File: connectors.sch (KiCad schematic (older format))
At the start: 40 parts, among them J10 70543-0001, J11 70543-0001, J12 70543-0001, J13 70543-0001, J14 70543-0003, J15 Conn_02x20_Odd_Even, J5 20021121-00010C4LF, J6 70543-0001, J7 70543-0001, J8 70543-0001, J9 70543-0001

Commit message: Current snapshot
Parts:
- renumbered C31 to C30, C32 to C31, C33 to C32, C34 to C33
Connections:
- net Z_OA1 renamed Z_BMB1
- net Z_OA2 renamed Z_BMB2
- net Z_OB1 renamed Z_BMA1
- net Z_OB2 renamed Z_BMA2
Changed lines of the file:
@@
 $Descr A4 11693 8268
 encoding utf-8
-Sheet 5 7
+Sheet 5 11
 Title "Connectors"
 Date ""
@@
 $EndComp
 $Comp
-L Device:C C31
+L Device:C C30
 U 1 1 5B1719D4
 P 1050 3450
-F 0 "C31" H 1165 3496 50  0000 L CNN
+F 0 "C30" H 1165 3496 50  0000 L CNN
 F 1 "100nF" H 1165 3405 50  0000 L CNN
 F 2 "Capacitor_SMD:C_0603_1608Metric" H 1088 3300 50  0001 C CNN
@@
 Text HLabel 4050 5700 0    50   Input ~ 0
 Y_MIN
-Text HLabel 4600 1300 0    50   Input ~ 0
-FAN1_OUT
 Text GLabel 4600 1400 0    50   Input ~ 0
 VDD_FAN
@@
 $EndComp
 Text HLabel 4600 3000 0    50   Input ~ 0
-Z_OA1
+Z_BMB1
 Text HLabel 4600 3100 0    50   Input ~ 0
-Z_OA2
+Z_BMB2
 Text HLabel 4600 3300 0    50   Input ~ 0
-Z_OB2
+Z_BMA2
 Text HLabel 4600 3200 0    50   Input ~ 0
-Z_OB1
-Text HLabel 4600 1600 0    50   Input ~ 0
-FAN2_OUT
+Z_BMA1
 Text GLabel 4600 1700 0    50   Input ~ 0
 VDD_FAN
@@
 	2150 4500 2150 4400
 $Comp
-L Device:C C32
+L Device:C C31
 U 1 1 5B56580A
 P 1050 4650
-F 0 "C32" H 1165 4696 50  0000 L CNN
+F 0 "C31" H 1165 4696 50  0000 L CNN
 F 1 "100nF" H 1165 4605 50  0000 L CNN
 F 2 "Capacitor_SMD:C_0603_1608Metric" H 1088 4500 50  0001 C CNN
@@
 	2150 5700 2150 5600
 $Comp
-L Device:C C33
+L Device:C C32
 U 1 1 5B57C5D0
 P 1050 5850
-F 0 "C33" H 1165 5896 50  0000 L CNN
+F 0 "C32" H 1165 5896 50  0000 L CNN
 F 1 "100nF" H 1165 5805 50  0000 L CNN
 F 2 "Capacitor_SMD:C_0603_1608Metric" H 1088 5700 50  0001 C CNN
@@
 	2150 6900 2150 6800
 $Comp
-L Device:C C34
+L Device:C C33
 U 1 1 5BC983BD
 P 1050 7050
-F 0 "C34" H 1165 7096 50  0000 L CNN
+F 0 "C33" H 1165 7096 50  0000 L CNN
 F 1 "100nF" H 1165 7005 50  0000 L CNN
 F 2 "Capacitor_SMD:C_0603_1608Metric" H 1088 6900 50  0001 C CNN
@@
 	1    0    0    -1
 $EndComp
-Text HLabel 4600 1900 0    50   Input ~ 0
-FAN3_OUT
 Text GLabel 4600 2000 0    50   Input ~ 0
 VDD_FAN
-Text HLabel 4600 2200 0    50   Input ~ 0
-FAN4_OUT
 Text GLabel 4600 2300 0    50   Input ~ 0
 VDD_FAN
@@
 	1    0    0    -1
 $EndComp
+Text GLabel 4600 1300 0    50   Input ~ 0
+FAN1_OUT
+Text GLabel 4600 1600 0    50   Input ~ 0
+FAN2_OUT
+Text GLabel 4600 1900 0    50   Input ~ 0
+FAN3_OUT
+Text GLabel 4600 2200 0    50   Input ~ 0
+FAN4_OUT
 $EndSCHEMATC

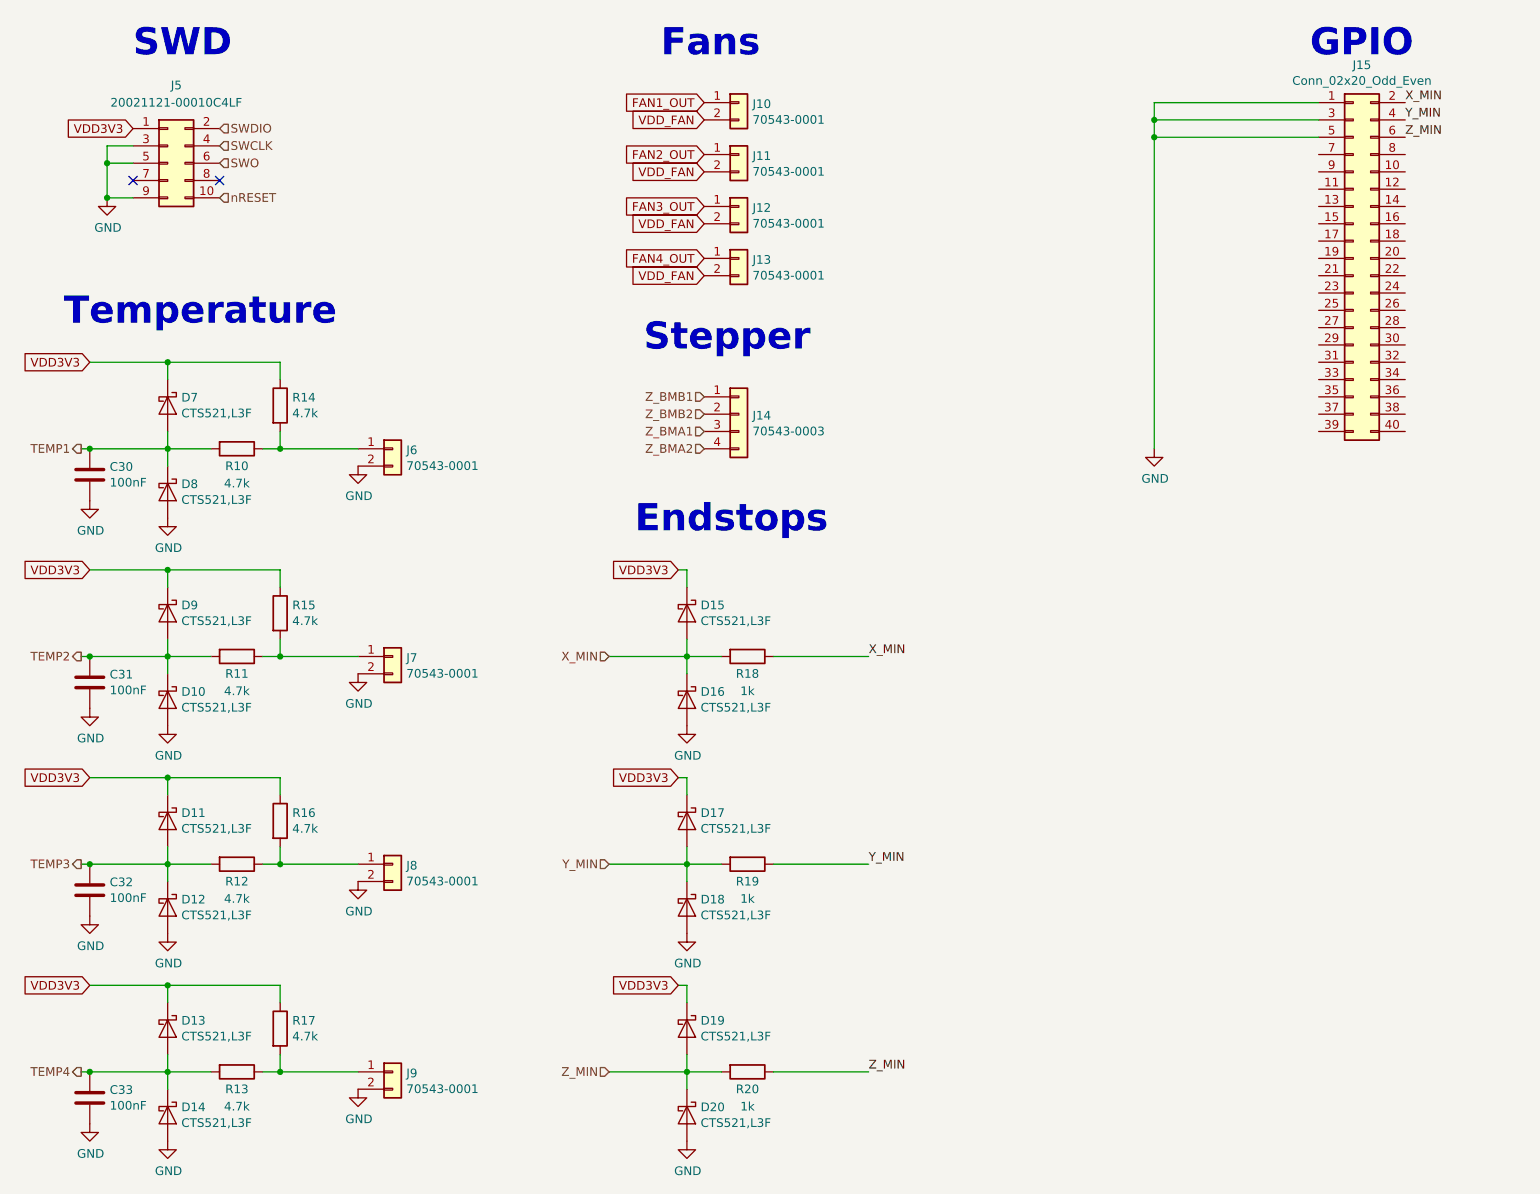
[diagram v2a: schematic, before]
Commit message: Placed last connectors
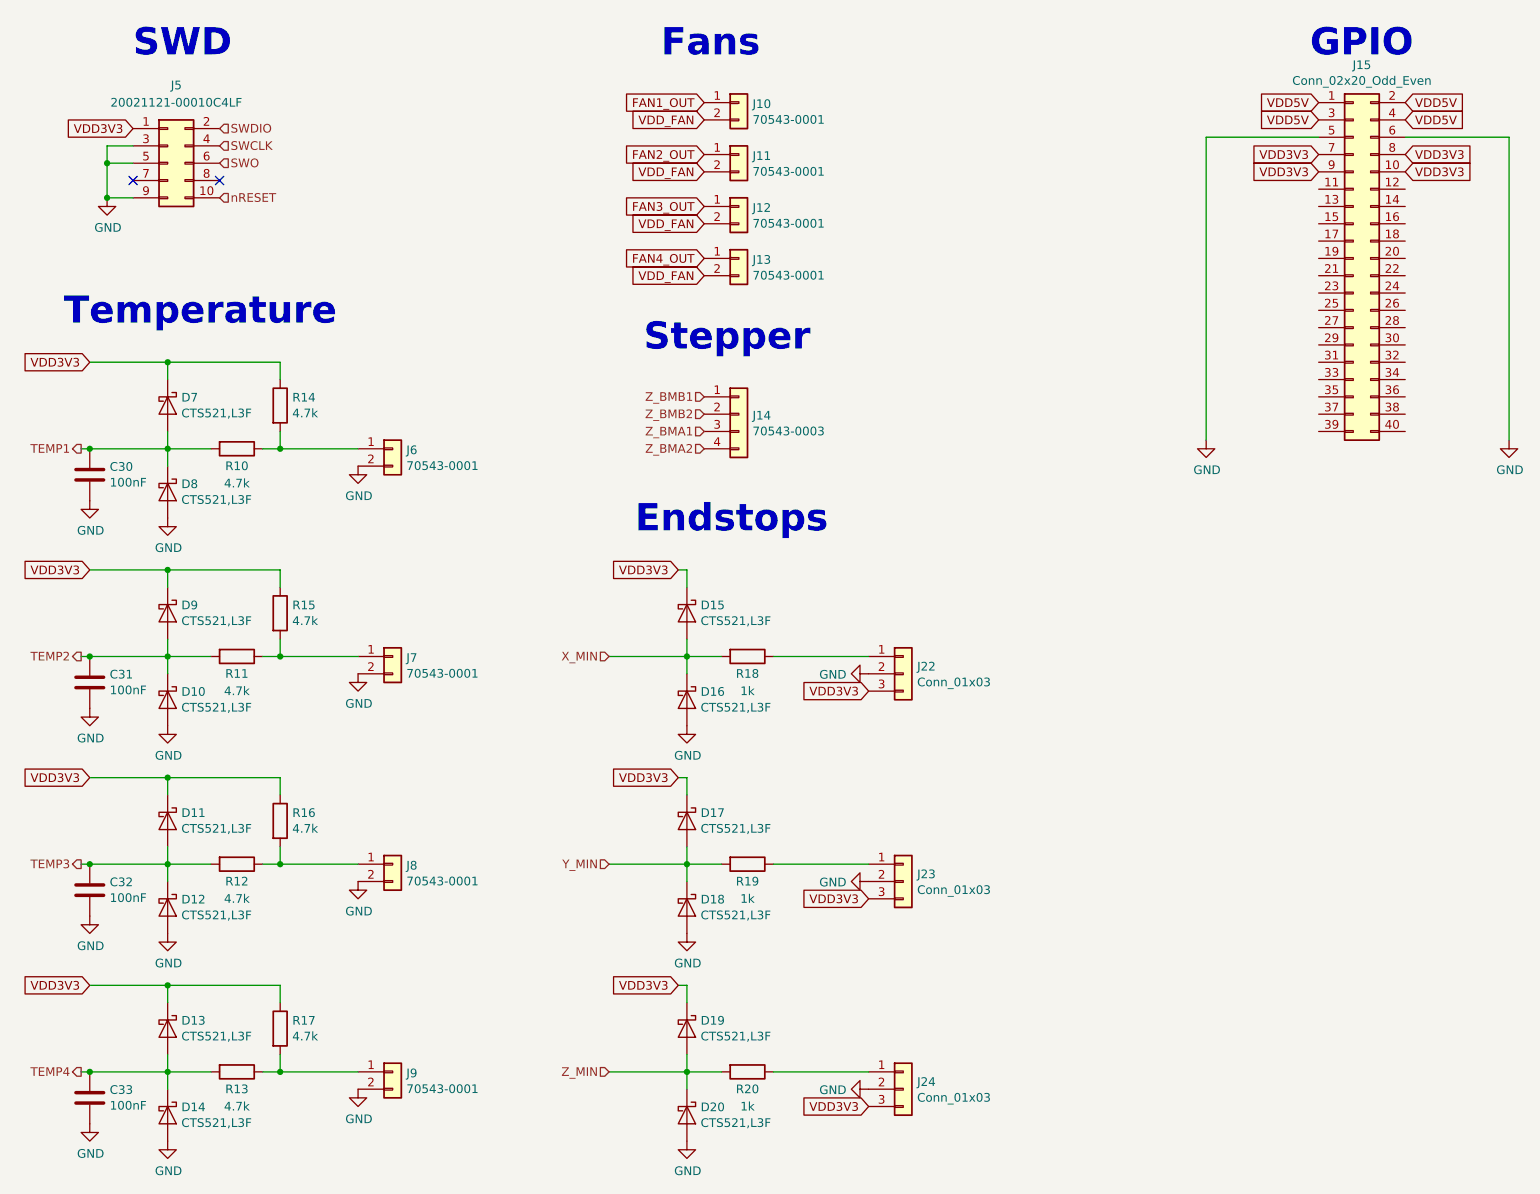
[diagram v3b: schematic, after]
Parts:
- added J22, J23, J24: Conn_01x03, heteromycin:70543-0002, symbol Connector_Generic:Conn_01x03
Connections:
- net GND: now also J15.6 (Pin_6), J22.2 (Pin_2), J23.2 (Pin_2), J24.2 (Pin_2); no longer J15.1 (Pin_1), J15.3 (Pin_3)
- net VDD3V3: now also J15.10 (Pin_10), J15.7 (Pin_7), J15.8 (Pin_8), J15.9 (Pin_9), J22.3 (Pin_3), J23.3 (Pin_3), J24.3 (Pin_3)
- net X_MIN: no longer J15.2 (Pin_2), R18.1
- net Y_MIN: no longer J15.4 (Pin_4), R19.1
- net Z_MIN: no longer J15.6 (Pin_6), R20.1
- new net: J22.1 (Pin_1), R18.1
- new net: J23.1 (Pin_1), R19.1
- new net: J24.1 (Pin_1), R20.1
- new net VDD5V: J15.1 (Pin_1), J15.2 (Pin_2), J15.3 (Pin_3), J15.4 (Pin_4)
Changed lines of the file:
@@
 	1    0    0    -1
 $EndComp
-Text Label 5550 4500 0    50   ~ 0
-X_MIN
-Text Label 5550 5700 0    50   ~ 0
-Y_MIN
-Text Label 5550 6900 0    50   ~ 0
-Z_MIN
-Text Label 8650 1300 0    50   ~ 0
-X_MIN
-Text Label 8650 1400 0    50   ~ 0
-Y_MIN
-Text Label 8650 1500 0    50   ~ 0
-Z_MIN
-$Comp
-L power:GND #PWR061
-U 1 1 5BD3671D
-P 7200 3300
-F 0 "#PWR061" H 7200 3050 50  0001 C CNN
-F 1 "GND" H 7205 3127 50  0000 C CNN
-F 2 "" H 7200 3300 50  0001 C CNN
-F 3 "" H 7200 3300 50  0001 C CNN
-	1    7200 3300
-	1    0    0    -1
-$EndComp
-Wire Wire Line
-	7200 3300 7200 1500
-Wire Wire Line
-	7200 1300 8150 1300
-Connection ~ 7200 1400
-Wire Wire Line
-	7200 1400 7200 1300
-Wire Wire Line
-	7200 1400 8150 1400
-Wire Wire Line
-	8150 1500 7200 1500
-Connection ~ 7200 1500
-Wire Wire Line
-	7200 1500 7200 1400
 $Comp
 L Connector_Generic:Conn_01x02 J11
@@
 Text GLabel 4600 2200 0    50   Input ~ 0
 FAN4_OUT
+$Comp
+L Connector_Generic:Conn_01x03 J22
+U 1 1 5BCA3C01
+P 5750 4600
+F 0 "J22" H 5830 4642 50  0000 L CNN
+F 1 "Conn_01x03" H 5830 4551 50  0000 L CNN
+F 2 "heteromycin:70543-0002" H 5750 4600 50  0001 C CNN
+F 3 "~" H 5750 4600 50  0001 C CNN
+	1    5750 4600
+	1    0    0    -1
+$EndComp
+$Comp
+L Connector_Generic:Conn_01x03 J23
+U 1 1 5BCAFD14
+P 5750 5800
+F 0 "J23" H 5830 5842 50  0000 L CNN
+F 1 "Conn_01x03" H 5830 5751 50  0000 L CNN
+F 2 "heteromycin:70543-0002" H 5750 5800 50  0001 C CNN
+F 3 "~" H 5750 5800 50  0001 C CNN
+	1    5750 5800
+	1    0    0    -1
+$EndComp
+$Comp
+L Connector_Generic:Conn_01x03 J24
+U 1 1 5BCB490A
+P 5750 7000
+F 0 "J24" H 5830 7042 50  0000 L CNN
+F 1 "Conn_01x03" H 5830 6951 50  0000 L CNN
+F 2 "heteromycin:70543-0002" H 5750 7000 50  0001 C CNN
+F 3 "~" H 5750 7000 50  0001 C CNN
+	1    5750 7000
+	1    0    0    -1
+$EndComp
+Text GLabel 5550 7100 0    50   Input ~ 0
+VDD3V3
+$Comp
+L power:GND #PWR072
+U 1 1 5BCB635E
+P 5550 7000
+F 0 "#PWR072" H 5550 6750 50  0001 C CNN
+F 1 "GND" V 5555 6872 50  0000 R CNN
+F 2 "" H 5550 7000 50  0001 C CNN
+F 3 "" H 5550 7000 50  0001 C CNN
+	1    5550 7000
+	0    1    1    0
+$EndComp
+$Comp
+L power:GND #PWR071
+U 1 1 5BCB65D2
+P 5550 5800
+F 0 "#PWR071" H 5550 5550 50  0001 C CNN
+F 1 "GND" V 5555 5672 50  0000 R CNN
+F 2 "" H 5550 5800 50  0001 C CNN
+F 3 "" H 5550 5800 50  0001 C CNN
+	1    5550 5800
+	0    1    1    0
+$EndComp
+Text GLabel 5550 5900 0    50   Input ~ 0
+VDD3V3
+Text GLabel 5550 4700 0    50   Input ~ 0
+VDD3V3
+$Comp
+L power:GND #PWR061
+U 1 1 5BCBB169
+P 5550 4600
+F 0 "#PWR061" H 5550 4350 50  0001 C CNN
+F 1 "GND" V 5555 4472 50  0000 R CNN
+F 2 "" H 5550 4600 50  0001 C CNN
+F 3 "" H 5550 4600 50  0001 C CNN
+	1    5550 4600
+	0    1    1    0
+$EndComp
+Text GLabel 8650 1300 2    50   Input ~ 0
+VDD5V
+Text GLabel 8650 1400 2    50   Input ~ 0
+VDD5V
+Text GLabel 8150 1300 0    50   Input ~ 0
+VDD5V
+Text GLabel 8150 1400 0    50   Input ~ 0
+VDD5V
+$Comp
+L power:GND #PWR?
+U 1 1 5BCCC745
+P 7500 3250
+F 0 "#PWR?" H 7500 3000 50  0001 C CNN
+F 1 "GND" H 7505 3077 50  0000 C CNN
+F 2 "" H 7500 3250 50  0001 C CNN
+F 3 "" H 7500 3250 50  0001 C CNN
+	1    7500 3250
+	1    0    0    -1
+$EndComp
+$Comp
+L power:GND #PWR?
+U 1 1 5BCCC827
+P 9250 3250
+F 0 "#PWR?" H 9250 3000 50  0001 C CNN
+F 1 "GND" H 9255 3077 50  0000 C CNN
+F 2 "" H 9250 3250 50  0001 C CNN
+F 3 "" H 9250 3250 50  0001 C CNN
+	1    9250 3250
+	1    0    0    -1
+$EndComp
+Wire Wire Line
+	7500 3250 7500 1500
+Wire Wire Line
+	7500 1500 8150 1500
+Wire Wire Line
+	9250 3250 9250 1500
+Wire Wire Line
+	9250 1500 8650 1500
+Text GLabel 8150 1600 0    50   Input ~ 0
+VDD3V3
+Text GLabel 8650 1600 2    50   Input ~ 0
+VDD3V3
+Text GLabel 8150 1700 0    50   Input ~ 0
+VDD3V3
+Text GLabel 8650 1700 2    50   Input ~ 0
+VDD3V3
 $EndSCHEMATC

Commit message: Some small adjustments
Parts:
- J22, J23, J24: value Conn_01x03 -> 70543-0002
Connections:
- net GND: now also J15.11 (Pin_11), J15.12 (Pin_12), J15.35 (Pin_35), J15.36 (Pin_36)
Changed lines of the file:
@@
 $Descr A4 11693 8268
 encoding utf-8
-Sheet 5 12
+Sheet 12 12
 Title "Connectors"
 Date ""
@@
 	1    0    0    -1
 $EndComp
-Text HLabel 4600 3000 0    50   Input ~ 0
-Z_BMB1
-Text HLabel 4600 3100 0    50   Input ~ 0
-Z_BMB2
-Text HLabel 4600 3300 0    50   Input ~ 0
-Z_BMA2
-Text HLabel 4600 3200 0    50   Input ~ 0
-Z_BMA1
 Text GLabel 4600 1700 0    50   Input ~ 0
 VDD_FAN
@@
 P 5750 4600
 F 0 "J22" H 5830 4642 50  0000 L CNN
-F 1 "Conn_01x03" H 5830 4551 50  0000 L CNN
+F 1 "70543-0002" H 5830 4551 50  0000 L CNN
 F 2 "heteromycin:70543-0002" H 5750 4600 50  0001 C CNN
 F 3 "~" H 5750 4600 50  0001 C CNN
@@
 P 5750 5800
 F 0 "J23" H 5830 5842 50  0000 L CNN
-F 1 "Conn_01x03" H 5830 5751 50  0000 L CNN
+F 1 "70543-0002" H 5830 5751 50  0000 L CNN
 F 2 "heteromycin:70543-0002" H 5750 5800 50  0001 C CNN
 F 3 "~" H 5750 5800 50  0001 C CNN
@@
 P 5750 7000
 F 0 "J24" H 5830 7042 50  0000 L CNN
-F 1 "Conn_01x03" H 5830 6951 50  0000 L CNN
+F 1 "70543-0002" H 5830 6951 50  0000 L CNN
 F 2 "heteromycin:70543-0002" H 5750 7000 50  0001 C CNN
 F 3 "~" H 5750 7000 50  0001 C CNN
@@
 VDD5V
 $Comp
-L power:GND #PWR?
+L power:GND #PWR0129
 U 1 1 5BCCC745
 P 7500 3250
-F 0 "#PWR?" H 7500 3000 50  0001 C CNN
+F 0 "#PWR0129" H 7500 3000 50  0001 C CNN
 F 1 "GND" H 7505 3077 50  0000 C CNN
 F 2 "" H 7500 3250 50  0001 C CNN
@@
 $EndComp
 $Comp
-L power:GND #PWR?
+L power:GND #PWR0130
 U 1 1 5BCCC827
 P 9250 3250
-F 0 "#PWR?" H 9250 3000 50  0001 C CNN
+F 0 "#PWR0130" H 9250 3000 50  0001 C CNN
 F 1 "GND" H 9255 3077 50  0000 C CNN
 F 2 "" H 9250 3250 50  0001 C CNN
@@
 $EndComp
 Wire Wire Line
-	7500 3250 7500 1500
+	7500 3250 7500 3000
 Wire Wire Line
 	7500 1500 8150 1500
 Wire Wire Line
-	9250 3250 9250 1500
+	9250 3250 9250 3000
 Wire Wire Line
 	9250 1500 8650 1500
@@
 Text GLabel 8650 1700 2    50   Input ~ 0
 VDD3V3
+Wire Wire Line
+	8650 3000 9250 3000
+Connection ~ 9250 3000
+Wire Wire Line
+	7500 3000 8150 3000
+Connection ~ 7500 3000
+Wire Wire Line
+	8650 1800 9250 1800
+Connection ~ 9250 1800
+Wire Wire Line
+	9250 1800 9250 1500
+Wire Wire Line
+	8150 1800 7500 1800
+Connection ~ 7500 1800
+Wire Wire Line
+	7500 1800 7500 1500
+Wire Wire Line
+	7500 1800 7500 3000
+Wire Wire Line
+	9250 1800 9250 3000
+Text HLabel 4600 3200 0    50   Input ~ 0
+Z_BMA1
+Text HLabel 4600 3300 0    50   Input ~ 0
+Z_BMA2
+Text HLabel 4600 3100 0    50   Input ~ 0
+Z_BMB2
+Text HLabel 4600 3000 0    50   Input ~ 0
+Z_BMB1
 $EndSCHEMATC

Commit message: First pass of routing
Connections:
- net GND: now also J15.33 (Pin_33), J15.34 (Pin_34); no longer J15.35 (Pin_35), J15.36 (Pin_36)
- net VDD3V3: now also J15.35 (Pin_35), J15.36 (Pin_36)
- net SCL: now reaches J15.13 (Pin_13)
- net SDA: now reaches J15.14 (Pin_14)
- net MCU_SCK: now reaches J15.15 (Pin_15)
- net PI_MOSI: now reaches J15.16 (Pin_16)
- net MCU_MISO: now reaches J15.17 (Pin_17)
- net PI_MISO: now reaches J15.18 (Pin_18)
- net MCU_MOSI: now reaches J15.19 (Pin_19)
- net PI_SCK: now reaches J15.20 (Pin_20)
- net MCU_D1: now reaches J15.21 (Pin_21)
- net PI_D1: now reaches J15.22 (Pin_22)
- net MCU_D2: now reaches J15.23 (Pin_23)
- net PI_D2: now reaches J15.24 (Pin_24)
- net MCU_D3: now reaches J15.25 (Pin_25)
- net PI_D3: now reaches J15.26 (Pin_26)
- net MCU_D4: now reaches J15.27 (Pin_27)
- net PI_D4: now reaches J15.28 (Pin_28)
- net MCU_D5: now reaches J15.29 (Pin_29)
- net PI_SS1: now reaches J15.30 (Pin_30)
- net TX: now reaches J15.31 (Pin_31)
- net RX: now reaches J15.32 (Pin_32)
- net PWM_EXT1: now reaches J15.37 (Pin_37)
- net PWM_EXT2: now reaches J15.38 (Pin_38)
- net PWM_EXT3: now reaches J15.39 (Pin_39)
- net PWM_EXT4: now reaches J15.40 (Pin_40)
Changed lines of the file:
@@
 $EndComp
 Wire Wire Line
-	7500 3250 7500 3000
-Wire Wire Line
 	7500 1500 8150 1500
-Wire Wire Line
-	9250 3250 9250 3000
 Wire Wire Line
 	9250 1500 8650 1500
@@
 VDD3V3
 Wire Wire Line
-	8650 3000 9250 3000
-Connection ~ 9250 3000
-Wire Wire Line
-	7500 3000 8150 3000
-Connection ~ 7500 3000
-Wire Wire Line
 	8650 1800 9250 1800
 Connection ~ 9250 1800
@@
 Wire Wire Line
 	7500 1800 7500 1500
-Wire Wire Line
-	7500 1800 7500 3000
-Wire Wire Line
-	9250 1800 9250 3000
 Text HLabel 4600 3200 0    50   Input ~ 0
 Z_BMA1
@@
 Text HLabel 4600 3000 0    50   Input ~ 0
 Z_BMB1
+Text HLabel 8150 3100 0    50   Input ~ 0
+PWM_EXT1
+Text HLabel 8650 3100 2    50   Input ~ 0
+PWM_EXT2
+Text HLabel 8150 3200 0    50   Input ~ 0
+PWM_EXT3
+Text HLabel 8650 3200 2    50   Input ~ 0
+PWM_EXT4
+Text HLabel 8650 1900 2    50   Input ~ 0
+SDA
+Text HLabel 8150 1900 0    50   Input ~ 0
+SCL
+Text HLabel 8150 2000 0    50   Input ~ 0
+MCU_SCK
+Text HLabel 8150 2200 0    50   Input ~ 0
+MCU_MOSI
+Text HLabel 8150 2100 0    50   Input ~ 0
+MCU_MISO
+Text HLabel 8150 2300 0    50   Input ~ 0
+MCU_D1
+Text HLabel 8150 2400 0    50   Input ~ 0
+MCU_D2
+Text HLabel 8150 2500 0    50   Input ~ 0
+MCU_D3
+Text HLabel 8150 2800 0    50   Input ~ 0
+TX
+Text HLabel 8650 2800 2    50   Input ~ 0
+RX
+Text HLabel 8150 2600 0    50   Input ~ 0
+MCU_D4
+Text HLabel 8150 2700 0    50   Input ~ 0
+MCU_D5
+Text HLabel 8650 2200 2    50   Input ~ 0
+PI_SCK
+Text HLabel 8650 2700 2    50   Input ~ 0
+PI_SS1
+Text HLabel 8650 2300 2    50   Input ~ 0
+PI_D1
+Text HLabel 8650 2400 2    50   Input ~ 0
+PI_D2
+Text HLabel 8650 2000 2    50   Input ~ 0
+PI_MOSI
+Text HLabel 8650 2100 2    50   Input ~ 0
+PI_MISO
+Text HLabel 8650 2500 2    50   Input ~ 0
+PI_D3
+Text HLabel 8650 2600 2    50   Input ~ 0
+PI_D4
+Wire Wire Line
+	7500 1800 7500 2900
+Wire Wire Line
+	9250 1800 9250 2900
+Text GLabel 8650 3000 2    50   Input ~ 0
+VDD3V3
+Text GLabel 8150 3000 0    50   Input ~ 0
+VDD3V3
+Wire Wire Line
+	8650 2900 9250 2900
+Connection ~ 9250 2900
+Wire Wire Line
+	9250 2900 9250 3250
+Wire Wire Line
+	8150 2900 7500 2900
+Connection ~ 7500 2900
+Wire Wire Line
+	7500 2900 7500 3250
 $EndSCHEMATC
